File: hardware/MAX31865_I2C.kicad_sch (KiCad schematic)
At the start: 1 part, among them U1 ATmega48A-A

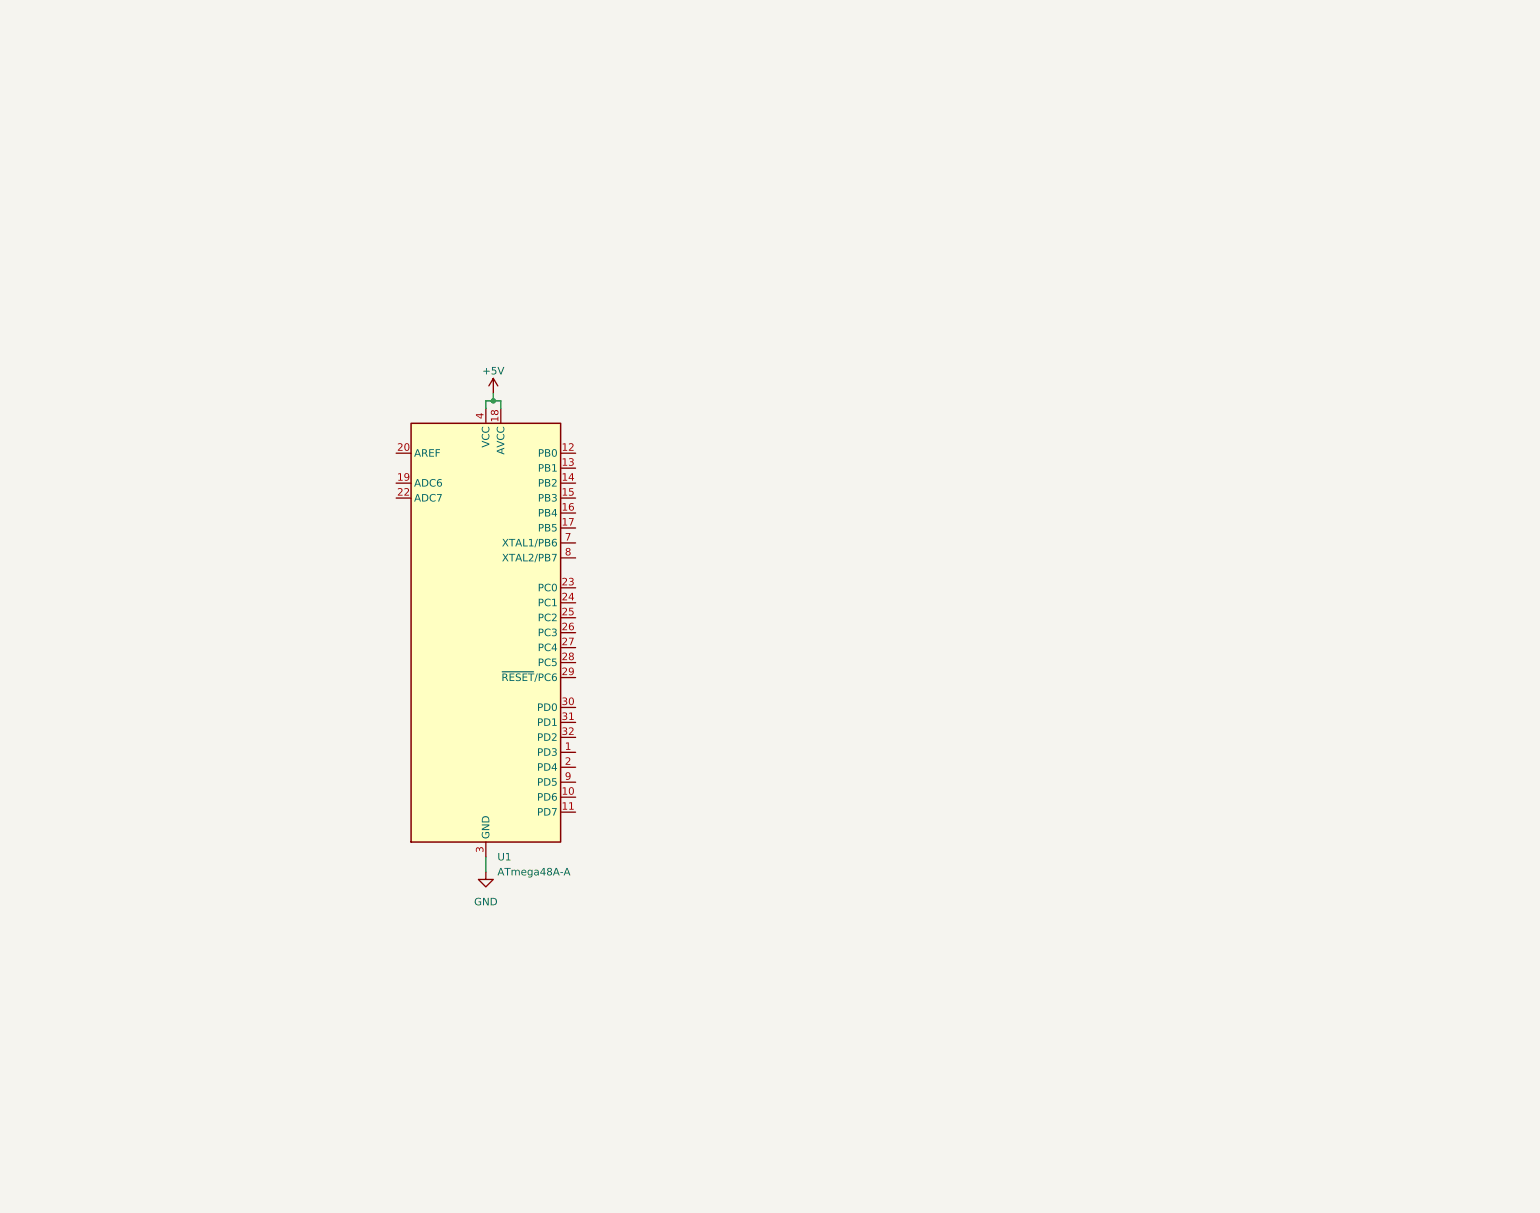
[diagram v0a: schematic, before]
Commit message: added rough sketch of the adapter PCB
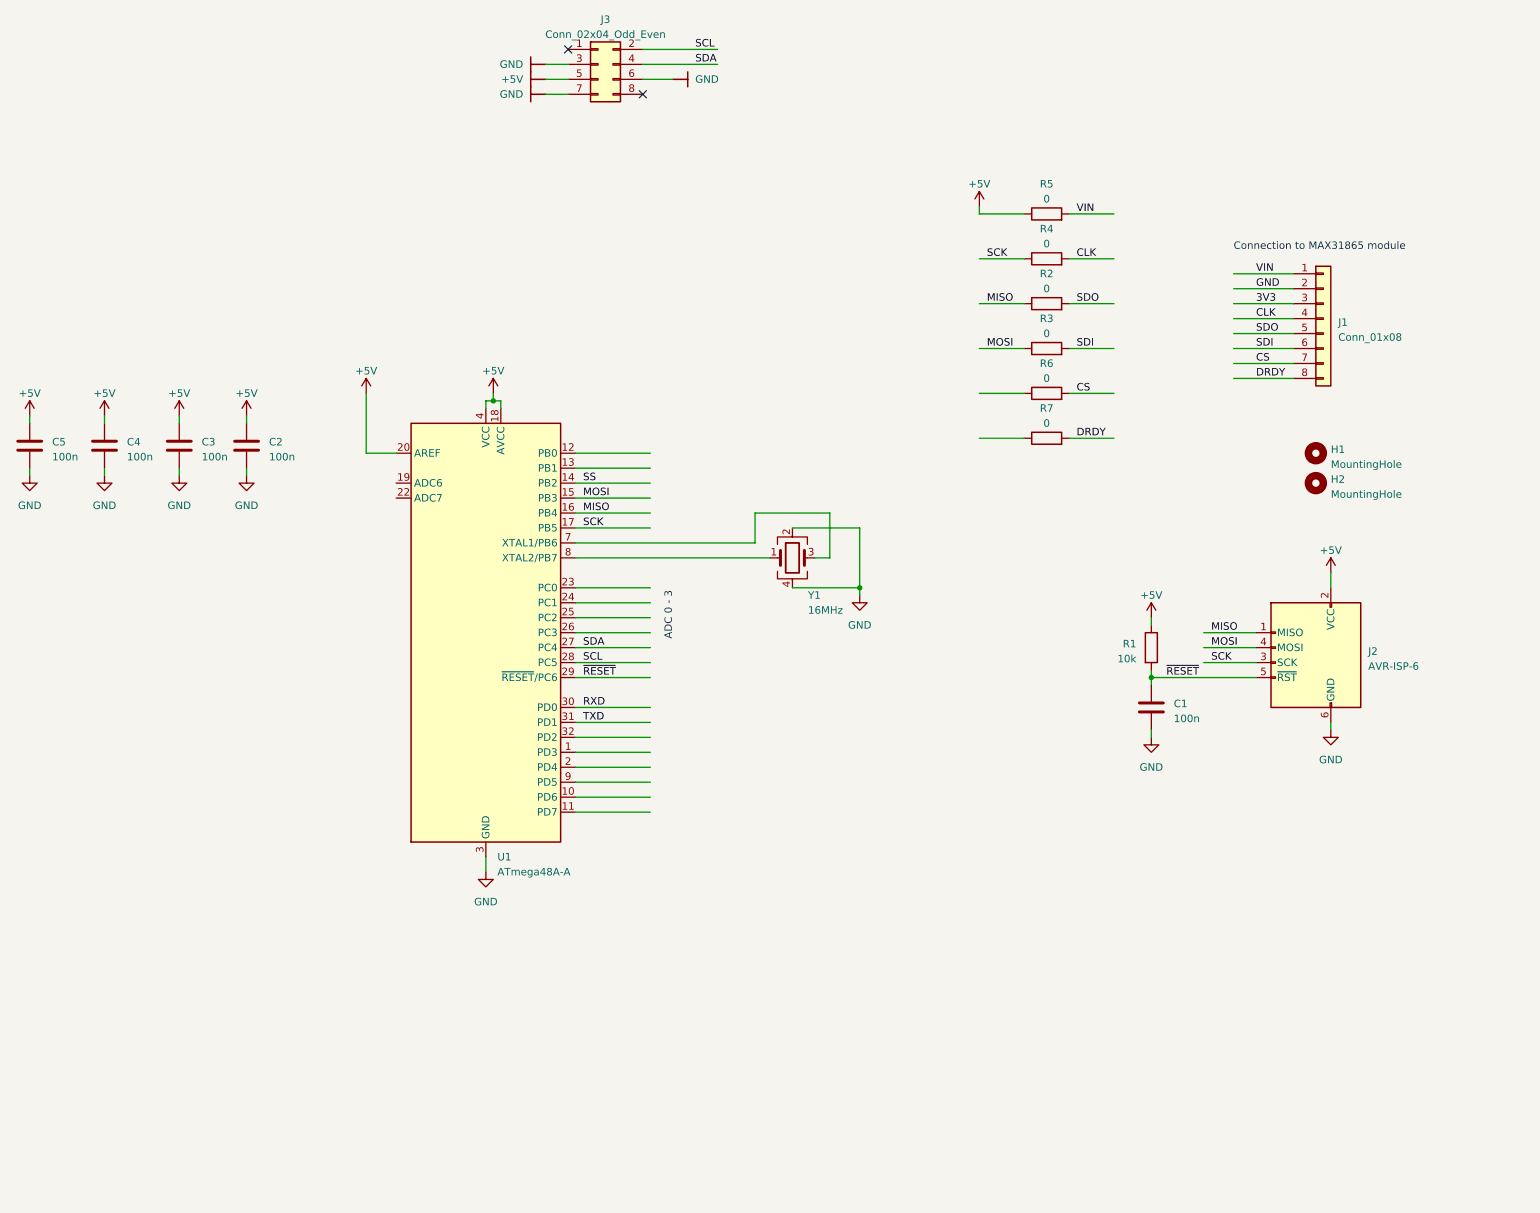
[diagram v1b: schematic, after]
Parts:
- added C1, C2, C3, C4, C5: 100n, Capacitor_SMD:C_0603_1608Metric, symbol Device:C
- added H1, H2: MountingHole, MountingHole:MountingHole_2.7mm, symbol Mechanical:MountingHole
- added J1: Conn_01x08, Connector_PinSocket_2.54mm:PinSocket_1x08_P2.54mm_Vertical, symbol Connector_Generic:Conn_01x08
- added J2: AVR-ISP-6, PinHeaderEdgeMount:PinHeader_2x03_P2.54mm_Edge, symbol Connector:AVR-ISP-6
- added J3: Conn_02x04_Odd_Even, PinHeaderEdgeMount:PinHeader_2x04_P2.54mm_Edge, symbol Connector_Generic:Conn_02x04_Odd_Even
- added R1: 10k, Resistor_SMD:R_0603_1608Metric, symbol Device:R
- added R2, R3, R4, R5, R6, R7: 0, Resistor_SMD:R_0603_1608Metric, symbol Device:R
- added Y1: 16MHz, Crystal:Crystal_SMD_EuroQuartz_MQ-4Pin_7.0x5.0mm, symbol Device:Crystal_GND24
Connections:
- net +5V: now also U1.20 (AREF), C2.1, C3.1, C4.1, C5.1, J2.2 (VCC), J3.5 (Pin_5), R1.1, R5.1
- net GND: now also C1.2, C2.2, C3.2, C4.2, C5.2, J1.2 (Pin_2), J2.6 (GND), J3.3 (Pin_3), J3.6 (Pin_6), J3.7 (Pin_7), Y1.2, Y1.4
- net SS: now reaches U1.14 (PB2)
- net MOSI: now reaches U1.15 (PB3)
- net MOSI: now also J2.4 (MOSI), R3.1
- net MISO: now reaches U1.16 (PB4)
- net MISO: now also J2.1 (MISO), R2.1
- net SCK: now reaches U1.17 (PB5)
- net SCK: now also J2.3 (SCK), R4.1
- net SDA: now reaches U1.27 (PC4)
- net SDA: now also J3.4 (Pin_4)
- net SCL: now reaches U1.28 (PC5)
- net SCL: now also J3.2 (Pin_2)
- net ~{RESET}: now reaches U1.29 (~{RESET}/PC6)
- net ~{RESET}: now also C1.1, J2.5 (~{RST}), R1.2
- net RXD: now reaches U1.30 (PD0)
- net TXD: now reaches U1.31 (PD1)
- net at U1.7 (XTAL1/PB6): now also Y1.3
- net at U1.8 (XTAL2/PB7): now also Y1.1
- new net 3V3: J1.3 (Pin_3)
- new net CLK: J1.4 (Pin_4), R4.2
- new net CS: J1.7 (Pin_7), R6.2
- new net DRDY: J1.8 (Pin_8), R7.2
- new net SDI: J1.6 (Pin_6), R3.2
- new net SDO: J1.5 (Pin_5), R2.2
- new net VIN: J1.1 (Pin_1), R5.2
- no-connect marks 0 -> 2
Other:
- note added: "ADC 0 - 3"
- note added: "Connection to MAX31865 module"

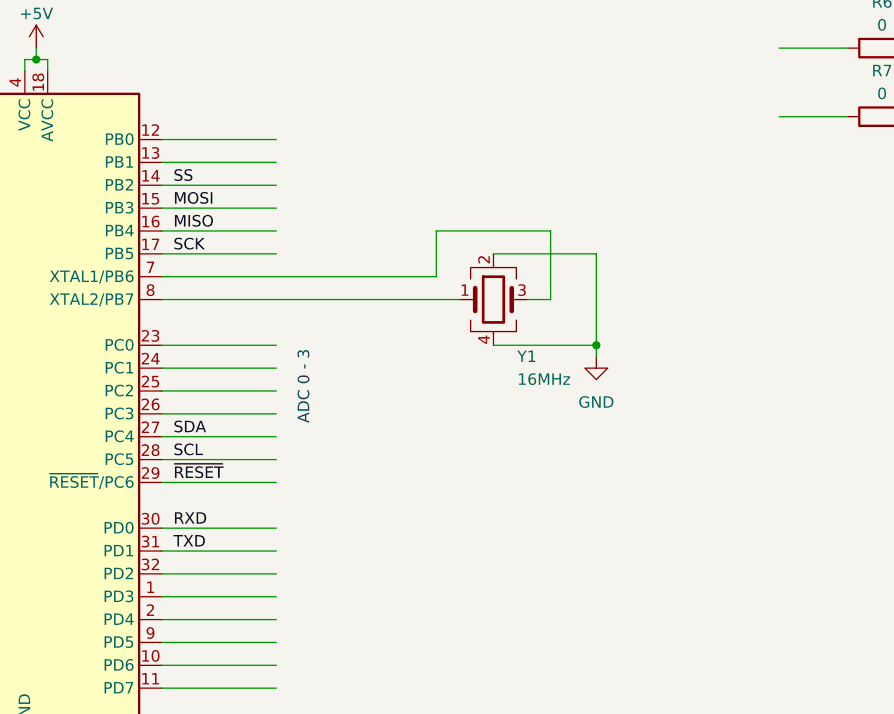
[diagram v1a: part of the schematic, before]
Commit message: added caps for crystal
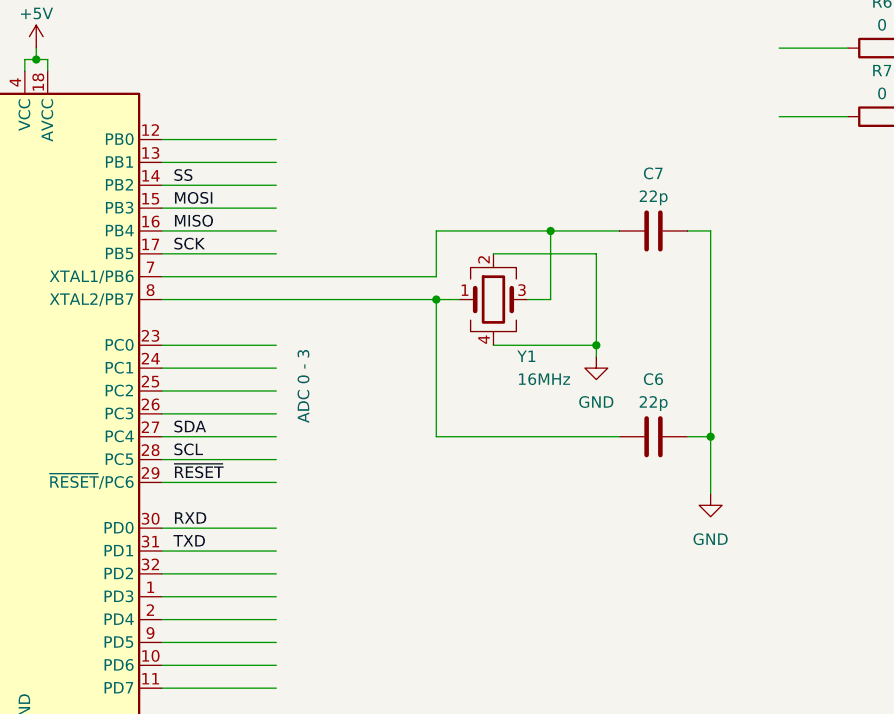
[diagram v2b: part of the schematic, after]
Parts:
- added C6, C7: 22p, Capacitor_SMD:C_0603_1608Metric, symbol Device:C
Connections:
- net GND: now also C6.2, C7.2
- net at U1.7 (XTAL1/PB6), Y1.3: now also C7.1
- net at U1.8 (XTAL2/PB7), Y1.1: now also C6.1
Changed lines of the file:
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@@
   (junction (at 217.17 93.98) (diameter 0) (color 0 0 0 0)
+  )
+  (junction (at 162.56 66.04) (diameter 0) (color 0 0 0 0)
+  )
+  (junction (at 149.86 73.66) (diameter 0) (color 0 0 0 0)
+  )
+  (junction (at 180.34 88.9) (diameter 0) (color 0 0 0 0)
   )
   (no_connect (at 118.11 -12.7))
@@
     (stroke (width 0) (type default))
   )
+  (wire (pts (xy 180.34 66.04) (xy 180.34 88.9))
+    (stroke (width 0) (type default))
+  )
   (wire (pts (xy 187.96 30.48) (xy 195.58 30.48))
     (stroke (width 0) (type default))
@@
     (stroke (width 0) (type default))
   )
+  (wire (pts (xy 149.86 73.66) (xy 152.4 73.66))
+    (stroke (width 0) (type default))
+  )
+  (wire (pts (xy 177.8 66.04) (xy 180.34 66.04))
+    (stroke (width 0) (type default))
+  )
   (wire (pts (xy 231.14 40.64) (xy 241.3 40.64))
     (stroke (width 0) (type default))
@@
     (stroke (width 0) (type default))
   )
+  (wire (pts (xy 180.34 88.9) (xy 180.34 95.25))
+    (stroke (width 0) (type default))
+  )
+  (wire (pts (xy 180.34 88.9) (xy 177.8 88.9))
+    (stroke (width 0) (type default))
+  )
   (wire (pts (xy 119.38 91.44) (xy 132.08 91.44))
     (stroke (width 0) (type default))
@@
     (stroke (width 0) (type default))
   )
+  (wire (pts (xy 149.86 88.9) (xy 149.86 73.66))
+    (stroke (width 0) (type default))
+  )
   (wire (pts (xy 104.14 48.26) (xy 104.14 46.99))
     (stroke (width 0) (type default))
@@
     (stroke (width 0) (type default))
   )
+  (wire (pts (xy 170.18 88.9) (xy 149.86 88.9))
+    (stroke (width 0) (type default))
+  )
   (wire (pts (xy 167.64 78.74) (xy 167.64 68.58))
     (stroke (width 0) (type default))
@@
     (stroke (width 0) (type default))
   )
-  (wire (pts (xy 119.38 73.66) (xy 152.4 73.66))
+  (wire (pts (xy 119.38 73.66) (xy 149.86 73.66))
     (stroke (width 0) (type default))
   )
@@
     (stroke (width 0) (type default))
   )
+  (wire (pts (xy 162.56 66.04) (xy 170.18 66.04))
+    (stroke (width 0) (type default))
+  )
   (wire (pts (xy 156.21 78.74) (xy 167.64 78.74))
     (stroke (width 0) (type default))
@@
         (path "/4d7972c0-b329-4137-a4d7-44898e682941"
           (reference "#PWR018") (unit 1)
+        )
+      )
+    )
+  )
+  (symbol (lib_id "PCM_4ms_Power-symbol:GND") (at 180.34 95.25 0) (unit 1)
+    (in_bom yes) (on_board yes) (dnp no) (fields_autoplaced)
+    (property "Reference" "#PWR022" (at 180.34 101.6 0)
+      (effects (font (size 1.27 1.27)) hide)
+    )
+    (property "Value" "GND" (at 180.34 100.33 0)
+      (effects (font (size 1.27 1.27)))
+    )
+    (property "Footprint" "" (at 180.34 95.25 0)
+      (effects (font (size 1.27 1.27)) hide)
+    )
+    (property "Datasheet" "" (at 180.34 95.25 0)
+      (effects (font (size 1.27 1.27)) hide)
+    )
+    (pin "1")
+    (instances
+      (project "MAX31865_I2C"
+        (path "/4d7972c0-b329-4137-a4d7-44898e682941"
+          (reference "#PWR022") (unit 1)
         )
       )
@@
     )
   )
+  (symbol (lib_id "Device:C") (at 173.99 88.9 90) (unit 1)
+    (in_bom yes) (on_board yes) (dnp no) (fields_autoplaced)
+    (property "Reference" "C6" (at 173.99 82.55 90)
+      (effects (font (size 1.27 1.27)))
+    )
+    (property "Value" "22p" (at 173.99 85.09 90)
+      (effects (font (size 1.27 1.27)))
+    )
+    (property "Footprint" "Capacitor_SMD:C_0603_1608Metric" (at 177.8 87.9348 0)
+      (effects (font (size 1.27 1.27)) hide)
+    )
+    (property "Datasheet" "~" (at 173.99 88.9 0)
+      (effects (font (size 1.27 1.27)) hide)
+    )
+    (pin "1")
+    (pin "2")
+    (instances
+      (project "MAX31865_I2C"
+        (path "/4d7972c0-b329-4137-a4d7-44898e682941"
+          (reference "C6") (unit 1)
+        )
+      )
+    )
+  )
   (symbol (lib_id "PCM_4ms_Power-symbol:GND") (at 52.07 59.69 0) (unit 1)
     (in_bom yes) (on_board yes) (dnp no) (fields_autoplaced)
@@
         )
       )
+    )
+  )
+  (symbol (lib_id "Device:C") (at 173.99 66.04 90) (unit 1)
+    (in_bom yes) (on_board yes) (dnp no) (fields_autoplaced)
+    (property "Reference" "C7" (at 173.99 59.69 90)
+      (effects (font (size 1.27 1.27)))
+    )
+    (property "Value" "22p" (at 173.99 62.23 90)
+      (effects (font (size 1.27 1.27)))
+    )
+    (property "Footprint" "Capacitor_SMD:C_0603_1608Metric" (at 177.8 65.0748 0)
+      (effects (font (size 1.27 1.27)) hide)
+    )
+    (property "Datasheet" "~" (at 173.99 66.04 0)
+      (effects (font (size 1.27 1.27)) hide)
+    )
+    (pin "1")
+    (pin "2")
+    (instances
+      (project "MAX31865_I2C"
+        (path "/4d7972c0-b329-4137-a4d7-44898e682941"
+          (reference "C7") (unit 1)
+        )
+      )
